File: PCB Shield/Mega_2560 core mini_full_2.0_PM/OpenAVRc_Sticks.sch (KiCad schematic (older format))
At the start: 61 parts, among them P11 Trim, P12 Stick_left, P13 Stick_right, P14 Switch, P23 Rot_1, P24 Rot_2, P25 Keys, P28 5v/3,3v manches, P31 Pot2, P32 Pot1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

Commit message: Replace P3_3V signal by +3,3V (solve no connected plane on top)
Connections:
- net P3_3V renamed +3.3V
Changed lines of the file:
@@
 Text Label 1200 6050 1    60   ~ 0
 Power_manches
-Text Label 3050 6150 1    60   ~ 0
-P3_3V
 $Comp
 L CONN_01X06 P13
@@
 Wire Wire Line
 	3700 4700 3700 4600
-Wire Wire Line
-	3050 5750 3050 6150
 Wire Wire Line
 	2950 6050 2950 5750
@@
 Text GLabel 9500 3950 1    60   Output ~ 0
 Stick_LH
+$Comp
+L +3,3V #PWR046
+U 1 1 59CA5E51
+P 3050 5850
+F 0 "#PWR046" H 3050 5810 30  0001 C CNN
+F 1 "+3,3V" H 3050 6000 39  0000 C CNN
+F 2 "" H 3050 5850 60  0001 C CNN
+F 3 "" H 3050 5850 60  0001 C CNN
+	1    3050 5850
+	-1   0    0    1
+$EndComp
+Wire Wire Line
+	3050 5850 3050 5750
 $EndSCHEMATC

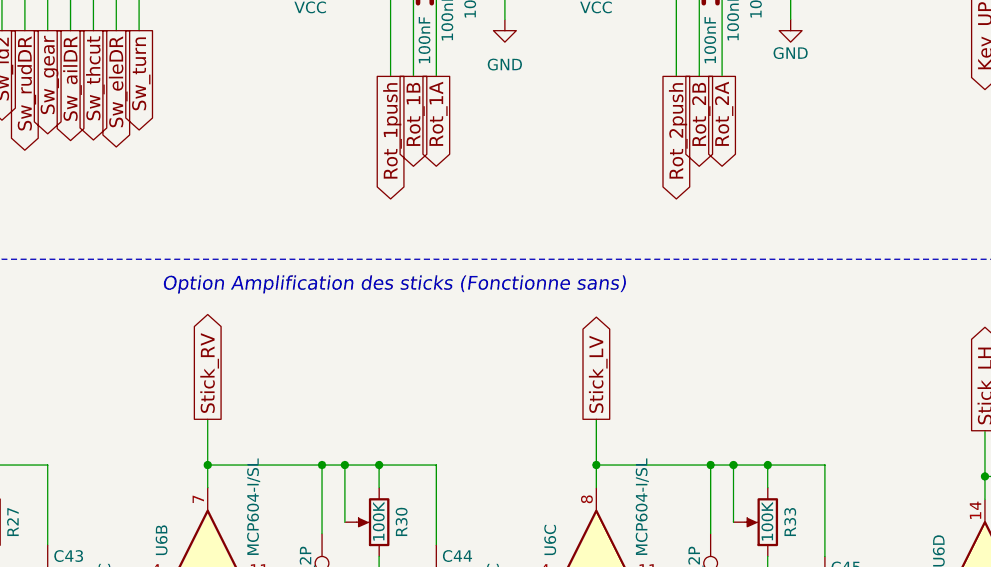
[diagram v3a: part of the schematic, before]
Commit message: Update schematic and pcb
Add PM-5033 as other dc/dc option
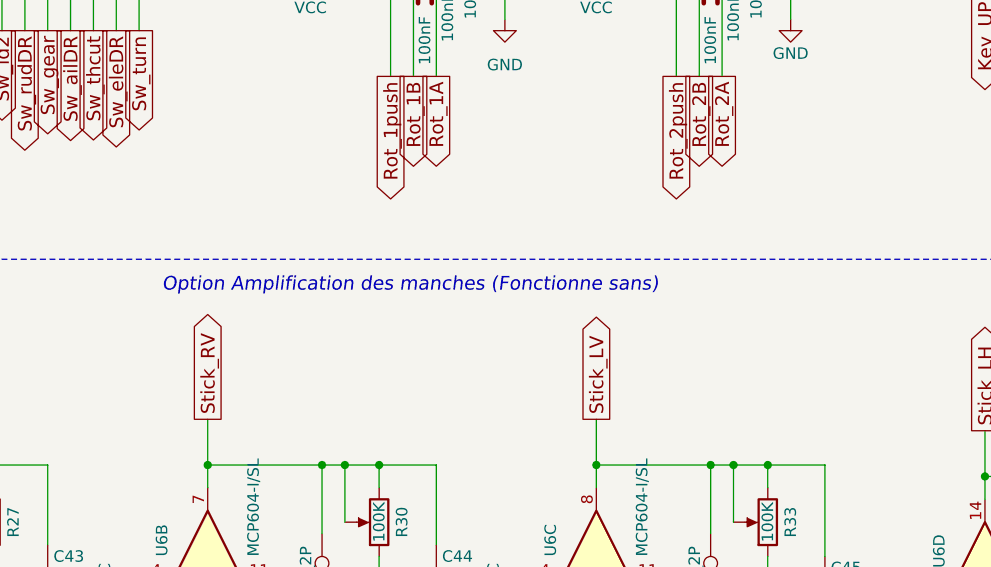
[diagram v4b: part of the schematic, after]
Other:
- note added: "Option Amplification des manches (Fonctionne sans)"
- note removed: "Option Amplification des sticks (Fonctionne sans)"
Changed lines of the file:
@@
 Sheet 2 7
 Title "Shield Mega2560 core Full"
-Date "2017-10-12"
+Date "2017-11-05"
 Rev "2.00"
 Comp ""
@@
 Stick control
 Text Notes 5900 3350 0    60   Italic 0
-Option Amplification des sticks (Fonctionne sans)
+Option Amplification des manches (Fonctionne sans)
 $Comp
 L TEST_2P W1

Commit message: Update shield files on good place
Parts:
- R18, R19, R22, R23: value 5.1k -> 5.1K
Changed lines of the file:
@@
 P 6700 1650
 F 0 "R19" V 6780 1650 50  0000 C CNN
-F 1 "5.1k" V 6700 1650 50  0000 C CNN
+F 1 "5.1K" V 6700 1650 50  0000 C CNN
 F 2 "Resistors_SMD:R_1206" V 6630 1650 50  0001 C CNN
 F 3 "" H 6700 1650 50  0000 C CNN
@@
 P 6700 1500
 F 0 "R18" V 6780 1500 50  0000 C CNN
-F 1 "5.1k" V 6700 1500 50  0000 C CNN
+F 1 "5.1K" V 6700 1500 50  0000 C CNN
 F 2 "Resistors_SMD:R_1206" V 6630 1500 50  0001 C CNN
 F 3 "" H 6700 1500 50  0000 C CNN
@@
 P 7950 1650
 F 0 "R23" V 8030 1650 50  0000 C CNN
-F 1 "5.1k" V 7950 1650 50  0000 C CNN
+F 1 "5.1K" V 7950 1650 50  0000 C CNN
 F 2 "Resistors_SMD:R_1206" V 7880 1650 50  0001 C CNN
 F 3 "" H 7950 1650 50  0000 C CNN
@@
 P 7950 1500
 F 0 "R22" V 8030 1500 50  0000 C CNN
-F 1 "5.1k" V 7950 1500 50  0000 C CNN
+F 1 "5.1K" V 7950 1500 50  0000 C CNN
 F 2 "Resistors_SMD:R_1206" V 7880 1500 50  0001 C CNN
 F 3 "" H 7950 1500 50  0000 C CNN

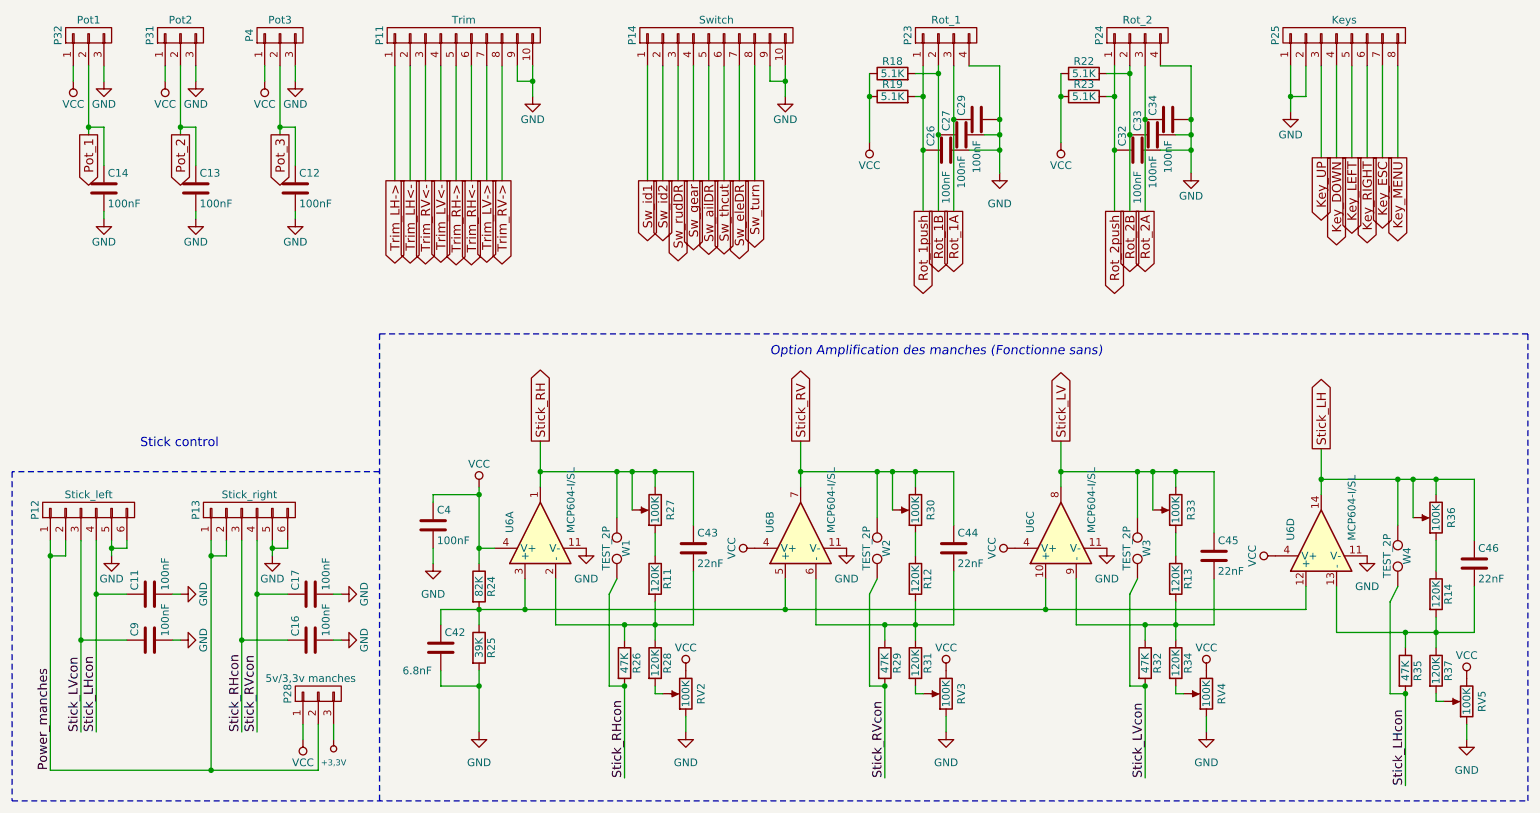
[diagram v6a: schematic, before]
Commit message: Re-update_shield_schéma
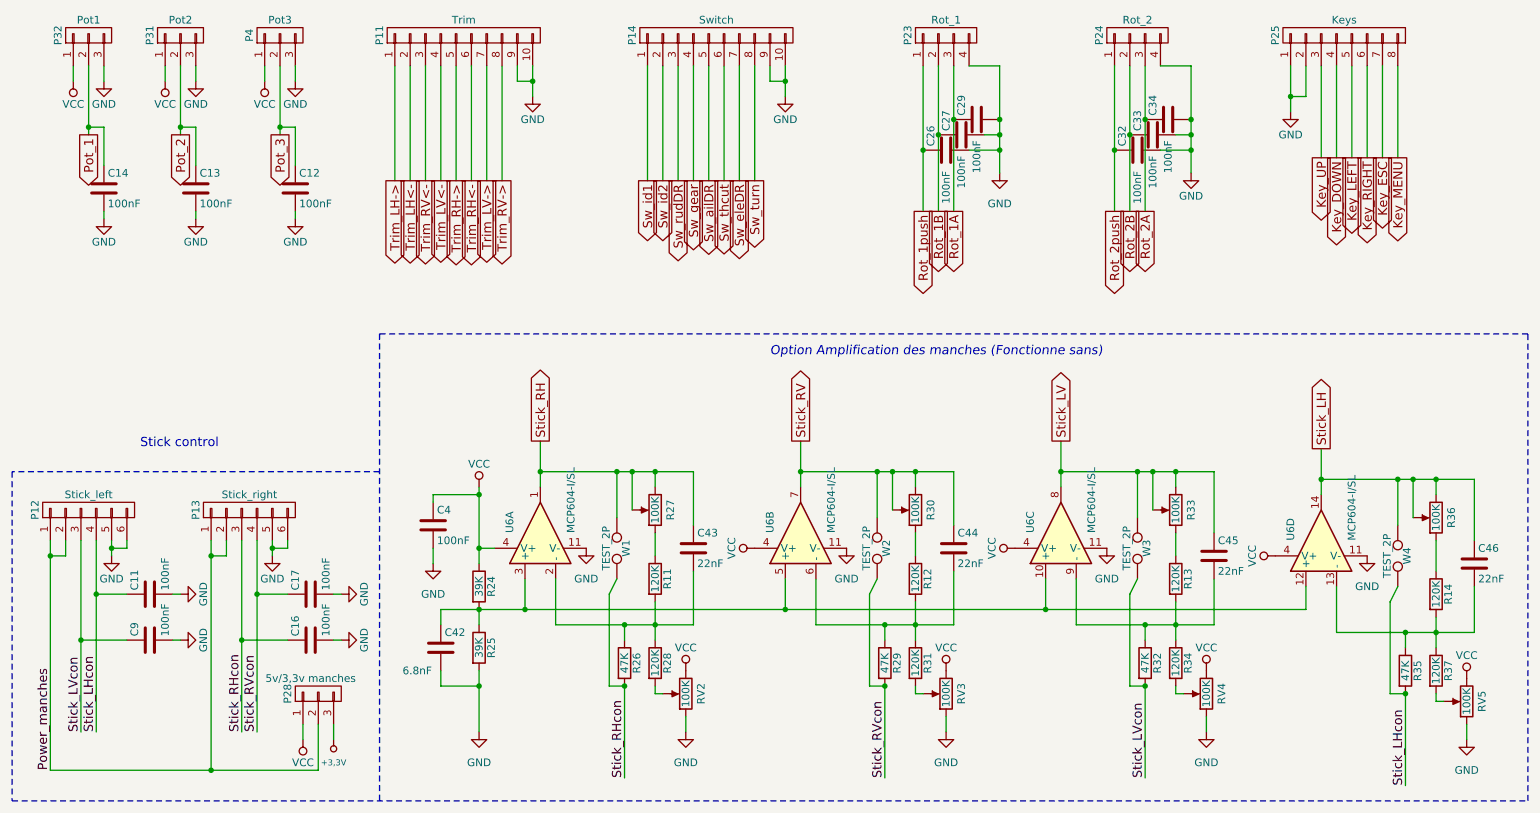
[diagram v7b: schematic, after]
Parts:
- removed R18, R19, R22, R23: 5.1K, Resistors_SMD:R_1206, symbol R-RESCUE-Mega_2560_core_mini_full_2.0
- R24: value 82K -> 39K
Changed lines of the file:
@@
 Sheet 2 7
 Title "Shield Mega2560 core Full"
-Date "2017-11-12"
+Date "2018-01-27"
 Rev "2.00"
 Comp "© Team OpenAVRc"
@@
 P 4000 4850
 F 0 "R24" V 4080 4850 50  0000 C CNN
-F 1 "82K" V 4000 4850 50  0000 C CNN
+F 1 "39K" V 4000 4850 50  0000 C CNN
 F 2 "Resistors_SMD:R_1206" V 3930 4850 50  0001 C CNN
 F 3 "" H 4000 4850 50  0000 C CNN
@@
 $EndComp
 $Comp
-L R-RESCUE-Mega_2560_core_mini_full_2.0 R19
-U 1 1 59C63F8D
-P 6700 1650
-F 0 "R19" V 6780 1650 50  0000 C CNN
-F 1 "5.1K" V 6700 1650 50  0000 C CNN
-F 2 "Resistors_SMD:R_1206" V 6630 1650 50  0001 C CNN
-F 3 "" H 6700 1650 50  0000 C CNN
-	1    6700 1650
-	0    -1   -1   0
-$EndComp
-$Comp
-L R-RESCUE-Mega_2560_core_mini_full_2.0 R18
-U 1 1 59C63F94
-P 6700 1500
-F 0 "R18" V 6780 1500 50  0000 C CNN
-F 1 "5.1K" V 6700 1500 50  0000 C CNN
-F 2 "Resistors_SMD:R_1206" V 6630 1500 50  0001 C CNN
-F 3 "" H 6700 1500 50  0000 C CNN
-	1    6700 1500
-	0    -1   -1   0
-$EndComp
-$Comp
-L R-RESCUE-Mega_2560_core_mini_full_2.0 R23
-U 1 1 59C63F9B
-P 7950 1650
-F 0 "R23" V 8030 1650 50  0000 C CNN
-F 1 "5.1K" V 7950 1650 50  0000 C CNN
-F 2 "Resistors_SMD:R_1206" V 7880 1650 50  0001 C CNN
-F 3 "" H 7950 1650 50  0000 C CNN
-	1    7950 1650
-	0    -1   -1   0
-$EndComp
-$Comp
-L R-RESCUE-Mega_2560_core_mini_full_2.0 R22
-U 1 1 59C63FA2
-P 7950 1500
-F 0 "R22" V 8030 1500 50  0000 C CNN
-F 1 "5.1K" V 7950 1500 50  0000 C CNN
-F 2 "Resistors_SMD:R_1206" V 7880 1500 50  0001 C CNN
-F 3 "" H 7950 1500 50  0000 C CNN
-	1    7950 1500
-	0    -1   -1   0
-$EndComp
-$Comp
-L VCC #PWR042
-U 1 1 59C63FA9
-P 6550 1950
-F 0 "#PWR042" H 6550 1800 50  0001 C CNN
-F 1 "VCC" H 6550 2100 50  0000 C CNN
-F 2 "" H 6550 1950 50  0000 C CNN
-F 3 "" H 6550 1950 50  0000 C CNN
-	1    6550 1950
-	-1   0    0    1
-$EndComp
-$Comp
-L VCC #PWR043
-U 1 1 59C63FAF
-P 7800 1950
-F 0 "#PWR043" H 7800 1800 50  0001 C CNN
-F 1 "VCC" H 7800 2100 50  0000 C CNN
-F 2 "" H 7800 1950 50  0000 C CNN
-F 3 "" H 7800 1950 50  0000 C CNN
-	1    7800 1950
-	-1   0    0    1
-$EndComp
-$Comp
 L CONN_01X08 P25
 U 1 1 59C63FBD
@@
 Wire Wire Line
 	7100 1450 7100 2400
-Connection ~ 6550 1650
-Wire Wire Line
-	6550 1500 6550 1950
-Connection ~ 7800 1650
-Wire Wire Line
-	7800 1500 7800 1950
-Connection ~ 8150 1650
-Wire Wire Line
-	8150 1650 8100 1650
-Connection ~ 8250 1500
-Wire Wire Line
-	8100 1500 8250 1500
 Wire Wire Line
 	8650 2000 8450 2000
@@
 Wire Wire Line
 	8450 1450 8650 1450
-Wire Wire Line
-	6850 1650 6900 1650
-Wire Wire Line
-	7000 1500 6850 1500
 Connection ~ 8650 1800
 Connection ~ 8350 1800
@@
 Connection ~ 7100 1800
 Connection ~ 8250 1900
-Connection ~ 6900 1650
-Connection ~ 7000 1500
 Wire Wire Line
 	7400 1450 7200 1450
